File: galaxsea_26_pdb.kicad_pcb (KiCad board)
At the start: 2 copper layers, 201 x 127.8 mm, 80 parts, among them J1 XT-30, J10 Screw Terminal Block, J11 Conn_01x36, J12 JST-XH, J13 Screw Terminal Block, J14 XT-30, J15 XT-30, J16 XT-30, J17 XT-30, J18 XT-30, J19 Conn_01x36, J2 XT-30, J20 JST-XH, J21 Screw Terminal Block, J22 XT-30, J23 XT-30, J24 XT-30, J25 Conn_01x36, J26 JST-XH, J27 Screw Terminal Block, J28 XT-30, J29 XT-30, J3 Conn_01x36, J30 XT-30, J4 Conn_01x36, J5 Conn_01x15_Socket, J6 Conn_01x15_Socket, J7 XT-90, J8 JST-XH, J9 XT-30, U1 TPS54531DDA, U2 TPS54531DDA

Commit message: Prepare for PDR
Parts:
- removed the G*** at (210.9, 33.4)
- added C27: 0.1u, Capacitor_SMD:C_0805_2012Metric, F.Cu at (90.6, 125.5)
- added C28: 10u, Capacitor_SMD:C_0805_2012Metric, F.Cu at (87.1, 125.5)
- added C29: 0.1u, Capacitor_SMD:C_0805_2012Metric, F.Cu at (61.4, 137.7)
- added C30: 0.1u, Capacitor_SMD:C_0805_2012Metric, F.Cu at (61.4, 105.5)
- added G***: LOGO, LOGO, B.Cu at (208.7, 36.0)
- added G***: LOGO, LOGO, B.Cu at (99.7, 94.1)
- added J31: XT-30, Connector_AMASS:AMASS_XT30UPB-F_1x02_P5.0mm_Vertical, F.Cu at (92.7, 146.1)
- added J32: XT-30, Connector_AMASS:AMASS_XT30UPB-F_1x02_P5.0mm_Vertical, F.Cu at (91.8, 60.8)
- added J33: XT-30, Connector_AMASS:AMASS_XT30UPB-F_1x02_P5.0mm_Vertical, F.Cu at (84.5, 60.8)
- J10, J13, J27: value Screw Terminal Block -> XT-30; footprint TerminalBlock:TerminalBlock_Altech_AK300-3_P5.00mm -> Connector_AMASS:AMASS_XT30UPB-F_1x02_P5.0mm_Vertical
- J12, J8: value JST-XH -> XT-30; footprint Connector_JST:JST_XH_B3B-XH-AM_1x03_P2.50mm_Vertical -> Connector_AMASS:AMASS_XT30UPB-F_1x02_P5.0mm_Vertical
- J20: value JST-XH -> XT-90; footprint Connector_JST:JST_XH_B3B-XH-AM_1x03_P2.50mm_Vertical -> footprints:XT90_V
- J21: value Screw Terminal Block -> Conn_01x36; footprint TerminalBlock:TerminalBlock_Altech_AK300-3_P5.00mm -> footprints:CONN_10018784_AMP
- J25: value Conn_01x36 -> XT-30; footprint footprints:CONN_10018784_AMP -> Connector_AMASS:AMASS_XT30UPB-F_1x02_P5.0mm_Vertical
- J26: value JST-XH -> Conn_01x36; footprint Connector_JST:JST_XH_B3B-XH-AM_1x03_P2.50mm_Vertical -> footprints:CONN_10018784_AMP
- J5: value Conn_01x15_Socket -> Conn_01x36; footprint Connector_PinHeader_2.54mm:PinHeader_1x15_P2.54mm_Vertical -> footprints:CONN_10018784_AMP
- J6: value Conn_01x15_Socket -> XT-30; footprint Connector_PinHeader_2.54mm:PinHeader_1x15_P2.54mm_Vertical -> Connector_AMASS:AMASS_XT30UPB-F_1x02_P5.0mm_Vertical
- moved H5 128.3 mm to (44.2, 57.7)
- moved H8 122.0 mm to (44.2, 148.7)
- moved J18 101.8 mm to (50.6, 79.0), turned to 0 degrees
- moved J16 91.9 mm to (127.3, 134.8)
- moved J10 87.2 mm to (127.3, 126.3), turned to 180 degrees
- moved J21 82.1 mm to (66.7, 143.5), turned to 90 degrees
- moved J12 76.6 mm to (50.6, 70.4)
- moved J27 75.4 mm to (50.6, 94.1), turned to 0 degrees
- moved J24 74.0 mm to (50.6, 134.8)
- moved J22 73.5 mm to (50.6, 126.3)
- moved C26 67.5 mm to (61.4, 73.4)
- moved J25 63.9 mm to (50.6, 143.3), turned to 0 degrees
- moved H6 61.2 mm to (133.4, 57.7)
- moved J20 56.4 mm to (88.9, 112.7), turned to 90 degrees
- moved J6 53.1 mm to (50.6, 61.9), turned to 0 degrees
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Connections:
- C21 pad 1: +BATT -> +ACT
- C22 pad 1: BDC2 -> /PDB/BDC2/VOUT
- C23 pad 1: BDC1 -> /PDB/BDC1/VOUT
- C24 pad 1: +BATT -> +ACT
- C25 pad 1: BDC3 -> /PDB/BDC3/VOUT
- C26 pad 1: BDC4 -> /PDB/BDC4/VOUT
- J10 pad 2: /PDB/SIG1 -> /PDB/BDC3/VOUT
- J11 pad A1: BDC1 -> /PDB/BDC1/VOUT
- J11 pad A10: BDC1 -> /PDB/BDC1/VOUT
- J11 pad A11: BDC1 -> /PDB/BDC1/VOUT
- J11 pad A2: BDC1 -> /PDB/BDC1/VOUT
- J11 pad A3: BDC1 -> /PDB/BDC1/VOUT
- J11 pad A4: BDC1 -> /PDB/BDC1/VOUT
- J11 pad A5: BDC1 -> /PDB/BDC1/VOUT
- J11 pad A6: BDC1 -> /PDB/BDC1/VOUT
- J11 pad A7: BDC1 -> /PDB/BDC1/VOUT
- J11 pad A8: BDC1 -> /PDB/BDC1/VOUT
- J11 pad A9: BDC1 -> /PDB/BDC1/VOUT
- J11 pad B1: +BATT -> +ACT
- J11 pad B10: +BATT -> +ACT
- J11 pad B11: +BATT -> +ACT
- J11 pad B2: +BATT -> +ACT
- J11 pad B3: +BATT -> +ACT
- J11 pad B4: +BATT -> +ACT
- J11 pad B5: +BATT -> +ACT
- J11 pad B6: +BATT -> +ACT
- J11 pad B7: +BATT -> +ACT
- J11 pad B8: +BATT -> +ACT
- J11 pad B9: +BATT -> +ACT
- J12 pad 2: /PDB/SIG2 -> /PDB/BDC4/VOUT
- J13 pad 2: /PDB/SIG2 -> /PDB/BDC1/VOUT
- J14 pad 2: BDC2 -> /PDB/BDC2/VOUT
- J15 pad 2: BDC1 -> /PDB/BDC1/VOUT
- J16 pad 2: BDC1 -> /PDB/BDC3/VOUT
- J17 pad 2: BDC2 -> /PDB/BDC2/VOUT
- J18 pad 2: BDC2 -> /PDB/BDC4/VOUT
- J19 pad A1: BDC3 -> /PDB/BDC3/VOUT
- J19 pad A10: BDC3 -> /PDB/BDC3/VOUT
- J19 pad A11: BDC3 -> /PDB/BDC3/VOUT
- J19 pad A2: BDC3 -> /PDB/BDC3/VOUT
- J19 pad A3: BDC3 -> /PDB/BDC3/VOUT
- J19 pad A4: BDC3 -> /PDB/BDC3/VOUT
- J19 pad A5: BDC3 -> /PDB/BDC3/VOUT
- J19 pad A6: BDC3 -> /PDB/BDC3/VOUT
- J19 pad A7: BDC3 -> /PDB/BDC3/VOUT
- J19 pad A8: BDC3 -> /PDB/BDC3/VOUT
- J19 pad A9: BDC3 -> /PDB/BDC3/VOUT
- J19 pad B1: +BATT -> +ACT
- J19 pad B10: +BATT -> +ACT
- J19 pad B11: +BATT -> +ACT
- J19 pad B2: +BATT -> +ACT
- J19 pad B3: +BATT -> +ACT
- J19 pad B4: +BATT -> +ACT
- J19 pad B5: +BATT -> +ACT
- J19 pad B6: +BATT -> +ACT
- J19 pad B7: +BATT -> +ACT
- J19 pad B8: +BATT -> +ACT
- J19 pad B9: +BATT -> +ACT
- J20 pad 2: /PDB/SIG3 -> +LOG
- J22 pad 2: BDC3 -> /PDB/BDC5/VOUT
- J23 pad 2: BDC3 -> /PDB/BDC3/VOUT
- J24 pad 2: BDC3 -> /PDB/BDC5/VOUT
- J27 pad 2: /PDB/SIG4 -> /PDB/BDC6/VOUT
- J28 pad 2: BDC4 -> /PDB/BDC6/VOUT
- J29 pad 2: BDC4 -> /PDB/BDC6/VOUT
- J3 pad A1: BDC2 -> /PDB/BDC2/VOUT
- J3 pad A10: BDC2 -> /PDB/BDC2/VOUT
- J3 pad A11: BDC2 -> /PDB/BDC2/VOUT
- J3 pad A2: BDC2 -> /PDB/BDC2/VOUT
- J3 pad A3: BDC2 -> /PDB/BDC2/VOUT
- J3 pad A4: BDC2 -> /PDB/BDC2/VOUT
- J3 pad A5: BDC2 -> /PDB/BDC2/VOUT
- J3 pad A6: BDC2 -> /PDB/BDC2/VOUT
- J3 pad A7: BDC2 -> /PDB/BDC2/VOUT
- J3 pad A8: BDC2 -> /PDB/BDC2/VOUT
- J3 pad A9: BDC2 -> /PDB/BDC2/VOUT
- J3 pad B1: +BATT -> +ACT
- J3 pad B10: +BATT -> +ACT
- J3 pad B11: +BATT -> +ACT
- J3 pad B2: +BATT -> +ACT
- J3 pad B3: +BATT -> +ACT
- J3 pad B4: +BATT -> +ACT
- J3 pad B5: +BATT -> +ACT
- J3 pad B6: +BATT -> +ACT
- J3 pad B7: +BATT -> +ACT
- J3 pad B8: +BATT -> +ACT
- J3 pad B9: +BATT -> +ACT
- J30 pad 2: BDC4 -> +LOG
- J6 pad 1: unconnected-(J6-Pin_1-Pad1) -> GND2
- J6 pad 2: unconnected-(J6-Pin_2-Pad2) -> /PDB/BDC4/VOUT
- J7 pad 2: +BATT -> +ACT
- J8 pad 2: /PDB/SIG1 -> /PDB/BDC1/VOUT
- J9 pad 2: BDC1 -> /PDB/BDC2/VOUT
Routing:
- net +BATT: track 179.3 -> 0.00 mm
- net +ACT: track 0.00 -> 165.3 mm
- net +LOG: track 0.00 -> 163.8 mm
- net BDC1: track 86.0 -> 0.00 mm
- net BDC4: track 72.5 -> 0.00 mm
- net BDC3: track 72.5 -> 0.00 mm
- net BDC2: track 72.5 -> 0.00 mm
- net /PDB/SIG3: track 60.2 -> 0.00 mm, vias 4 -> 0
- net /PDB/BDC3/VOUT: track 0.00 -> 49.9 mm
- net /PDB/BDC1/VOUT: track 0.00 -> 47.8 mm
- net /PDB/BDC6/VOUT: track 0.00 -> 46.6 mm
- net /PDB/BDC4/VOUT: track 0.00 -> 46.6 mm
- net /PDB/BDC5/VOUT: track 0.00 -> 46.6 mm
- net /PDB/SIG2: track 43.8 -> 0.00 mm, vias 2 -> 0
- net /PDB/SIG4: track 43.7 -> 0.00 mm, vias 2 -> 0
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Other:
- board size 201 x 127.8 mm -> 235.7 x 128.7 mm
- board text added: "Line A"
- board text added: "Line B"
- board text added: "Power Distribution Board Nathan Wignall ${CURRENT_DATE}"

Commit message: Finalize
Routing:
- net GND1: vias 108 -> 94
- added copper zone on F.Cu, net +ACT
- added copper zone on F.Cu, net +LOG
- added copper zone on F.Cu, net /PDB/BDC1/VOUT
- added copper zone on F.Cu, net /PDB/BDC2/VOUT
- added copper zone on F.Cu, net /PDB/BDC3/VOUT
- added copper zone on F.Cu, net /PDB/BDC4/VOUT
- added copper zone on F.Cu, net /PDB/BDC5/VOUT
- added copper zone on F.Cu, net /PDB/BDC6/VOUT

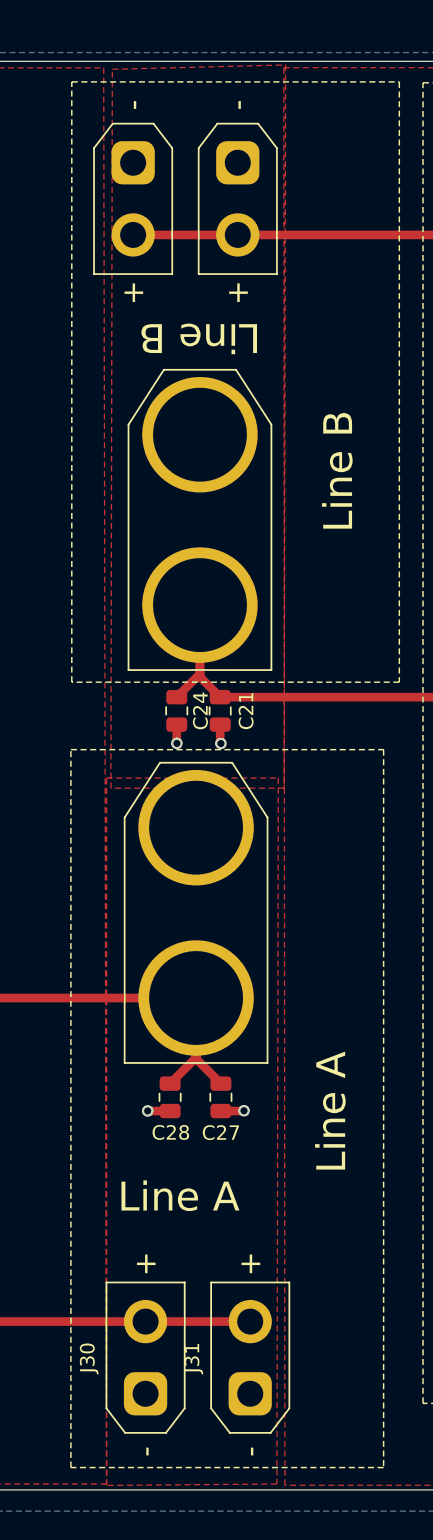
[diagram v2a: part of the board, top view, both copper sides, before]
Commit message: Add JST B2B-XH connectors
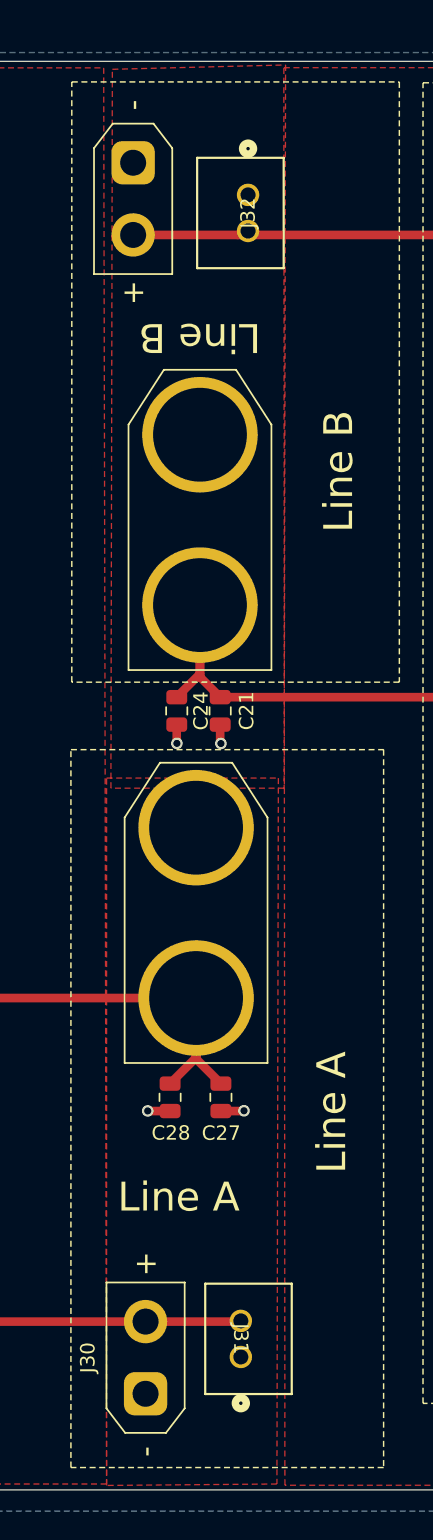
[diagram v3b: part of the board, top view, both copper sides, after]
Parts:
- J31, J32: footprint Connector_AMASS:AMASS_XT30UPB-F_1x02_P5.0mm_Vertical -> footprints:CONN_B2B-XH-ALFSN_JST
- moved J31 2.63 mm to (92.0, 143.5), turned to -90 degrees
- moved J32 2.34 mm to (92.5, 63.0), turned to 90 degrees
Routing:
- net +LOG: track 163.8 -> 163.2 mm

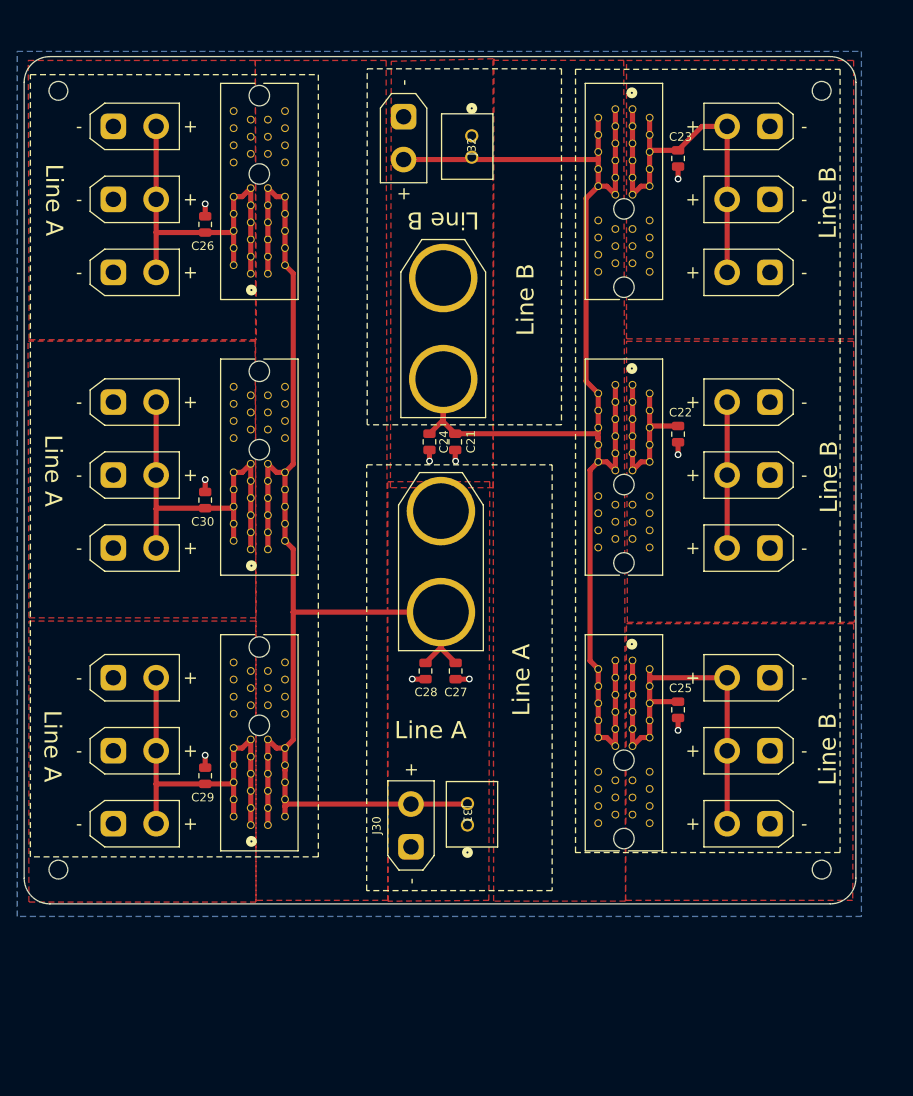
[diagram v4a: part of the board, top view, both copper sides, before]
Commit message: Add motor connectors
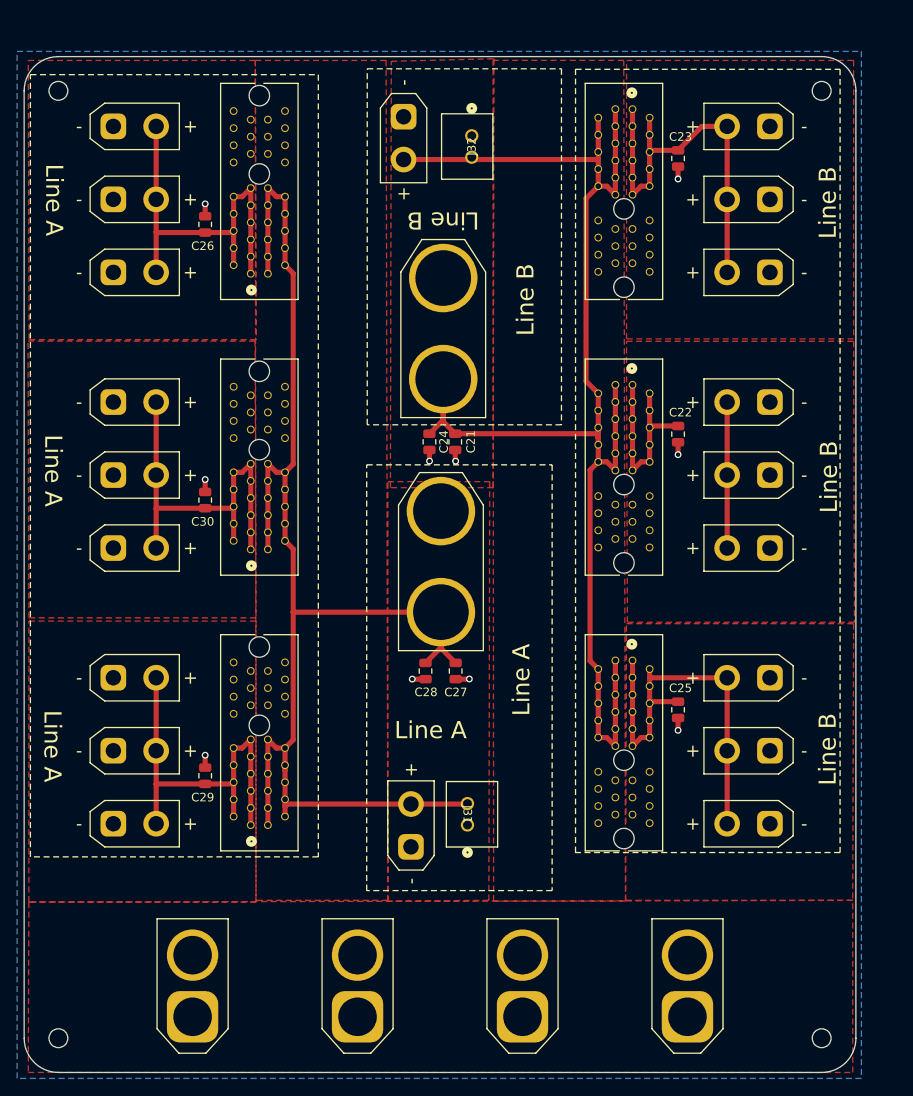
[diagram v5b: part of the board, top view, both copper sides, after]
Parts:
- added J34: XT-60, footprints:AMASS_XT60-F_1x02_P7.20mm_Vertical, F.Cu at (59.9, 165.9)
- added J35: XT-60, footprints:AMASS_XT60-F_1x02_P7.20mm_Vertical, F.Cu at (79.2, 165.9)
- added J36: XT-60, footprints:AMASS_XT60-F_1x02_P7.20mm_Vertical, F.Cu at (98.4, 165.9)
- added J37: XT-60, footprints:AMASS_XT60-F_1x02_P7.20mm_Vertical, F.Cu at (117.7, 165.9)
- J31, J32: value XT-30 -> B2B-XH
- moved H7 19.7 mm to (133.4, 168.4)
- moved H8 19.7 mm to (44.2, 168.4)
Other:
- board size 235.7 x 128.7 mm -> 235.7 x 148.4 mm
- board text added: "M2"

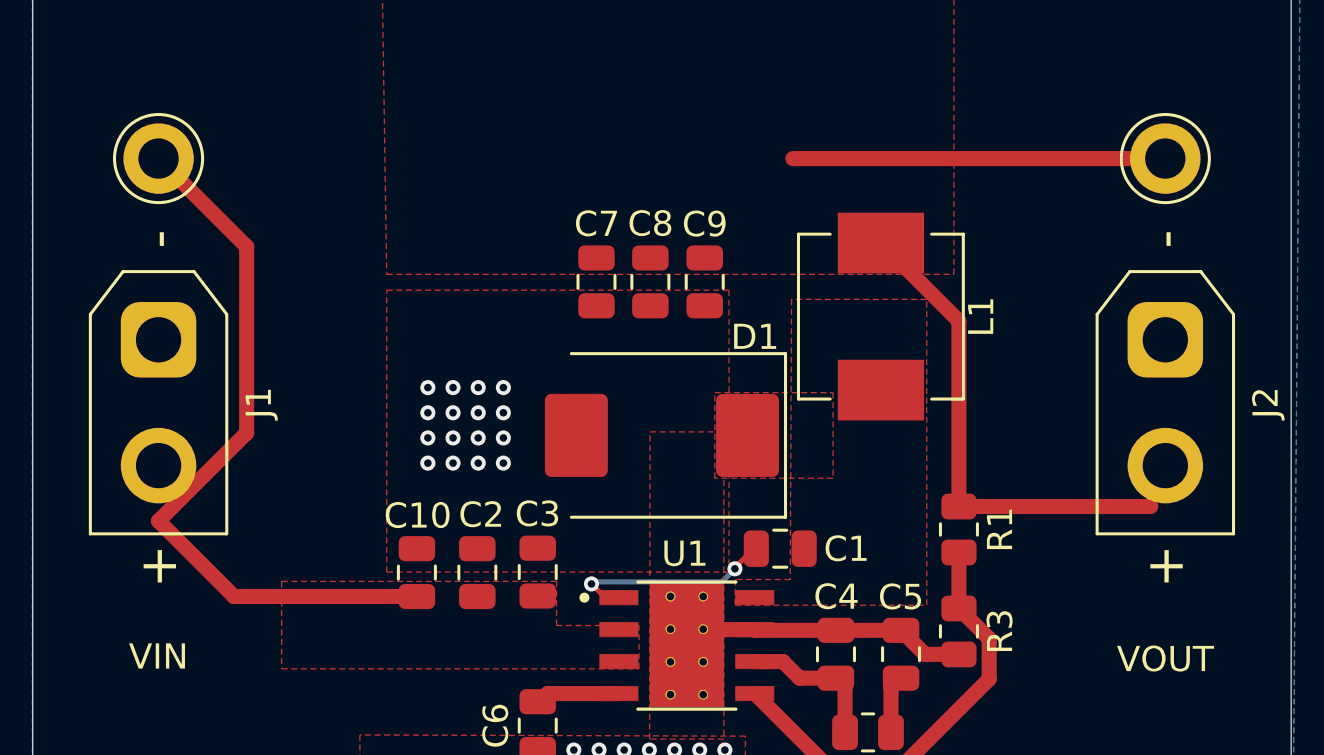
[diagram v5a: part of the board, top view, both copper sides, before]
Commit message: Update buck converter module silkscreen
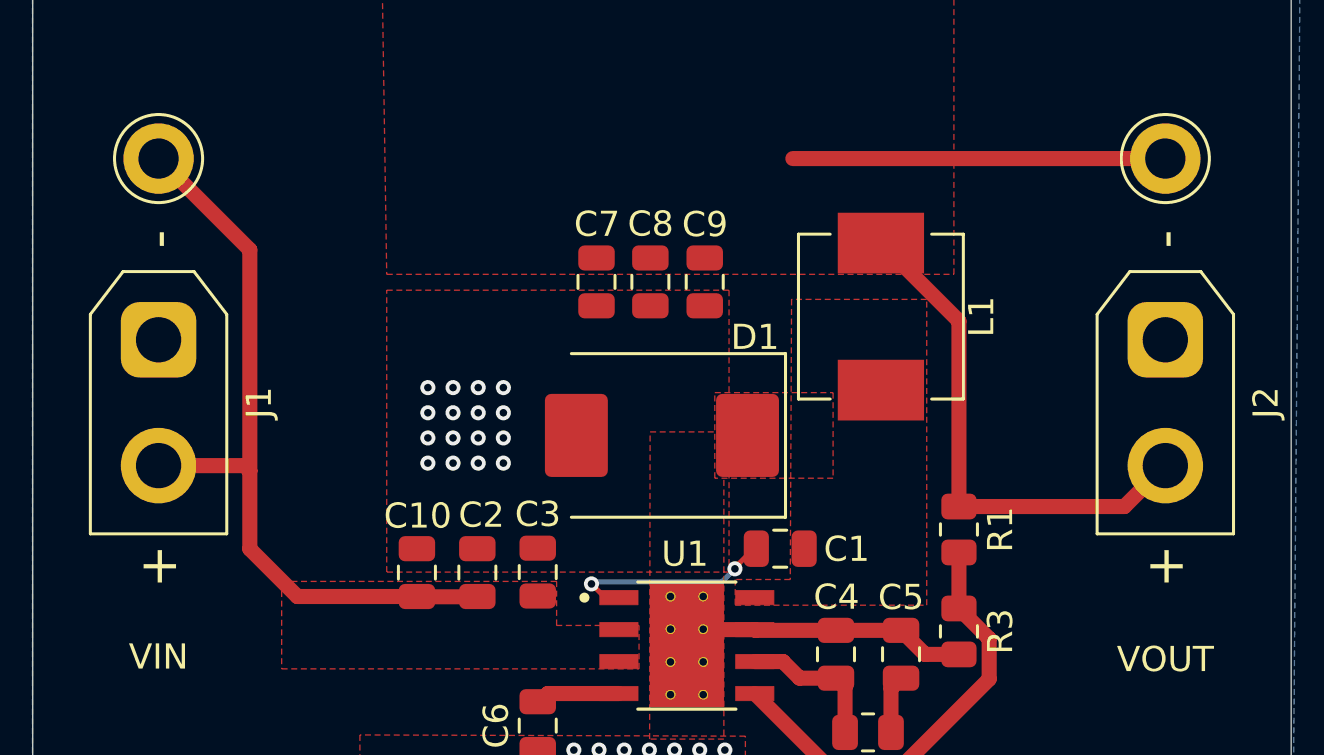
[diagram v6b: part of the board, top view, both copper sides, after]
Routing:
- net /BDC Test Module/VIN: track 28.8 -> 30.9 mm
- net /BDC Test Module/VOUT: track 34.2 -> 35.4 mm
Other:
- board text added: "TPS54531DDA Module Nathan Wignall ${CURRENT_DATE}"
- board text removed: "5V Buck Converter Module Nathan Wignall ${CURRENT_DATE}"
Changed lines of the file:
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@@
 		)
 	)
-	(gr_text "5V Buck Converter Module\nNathan Wignall\n${CURRENT_DATE}"
-		(at 213.635 44.364 -0)
+	(gr_text "TPS54531DDA Module\nNathan Wignall\n${CURRENT_DATE}"
+		(at 213.635 44.364 0)
 		(layer "B.SilkS")
 		(effects
@@
 	)
 	(segment
+		(start 269.249 52.014)
+		(end 270.874 50.389)
+		(width 0.6)
+		(layer "F.Cu")
+		(net "/BDC Test Module/VOUT")
+	)
+	(segment
+		(start 262.674 52.014)
+		(end 269.249 52.014)
+		(width 0.6)
+		(layer "F.Cu")
+		(net "/BDC Test Module/VOUT")
+	)
+	(segment
 		(start 262.674 44.647)
 		(end 259.574 41.547)
-		(width 0.6)
-		(layer "F.Cu")
-		(net "/BDC Test Module/VOUT")
-	)
-	(segment
-		(start 262.674 52.014)
-		(end 270.299 52.014)
 		(width 0.6)
 		(layer "F.Cu")
@@
 	)
 	(segment
-		(start 230.874 38.189)
-		(end 234.375 41.69)
+		(start 234.289 50.389)
+		(end 230.874 50.389)
 		(width 0.6)
 		(layer "F.Cu")
@@
 	)
 	(segment
-		(start 233.874 55.589)
+		(start 234.5 53.7)
+		(end 234.5 50.6)
+		(width 0.6)
+		(layer "F.Cu")
+		(net "/BDC Test Module/VIN")
+	)
+	(segment
+		(start 241.139 55.589)
+		(end 236.389 55.589)
+		(width 0.6)
+		(layer "F.Cu")
+		(net "/BDC Test Module/VIN")
+	)
+	(segment
+		(start 234.5 41.815)
+		(end 230.874 38.189)
+		(width 0.6)
+		(layer "F.Cu")
+		(net "/BDC Test Module/VIN")
+	)
+	(segment
+		(start 241.128 55.6)
 		(end 241.139 55.589)
 		(width 0.6)
@@
 	)
 	(segment
-		(start 230.874 52.589)
-		(end 233.874 55.589)
+		(start 234.5 50.6)
+		(end 234.289 50.389)
 		(width 0.6)
 		(layer "F.Cu")
@@
 	)
 	(segment
-		(start 234.375 41.69)
-		(end 234.375 49.088)
+		(start 234.5 50.6)
+		(end 234.5 41.815)
 		(width 0.6)
 		(layer "F.Cu")
@@
 	)
 	(segment
-		(start 234.375 49.088)
-		(end 230.874 52.589)
-		(width 0.6)
-		(layer "F.Cu")
+		(start 236.389 55.589)
+		(end 234.5 53.7)
+		(width 0.6)
+		(layer "F.Cu")
+		(net "/BDC Test Module/VIN")
+	)
+	(segment
+		(start 243.885 55.6)
+		(end 241.128 55.6)
+		(width 0.6)
+		(layer "F.Cu")
